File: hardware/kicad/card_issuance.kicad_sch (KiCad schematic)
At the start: 0 parts

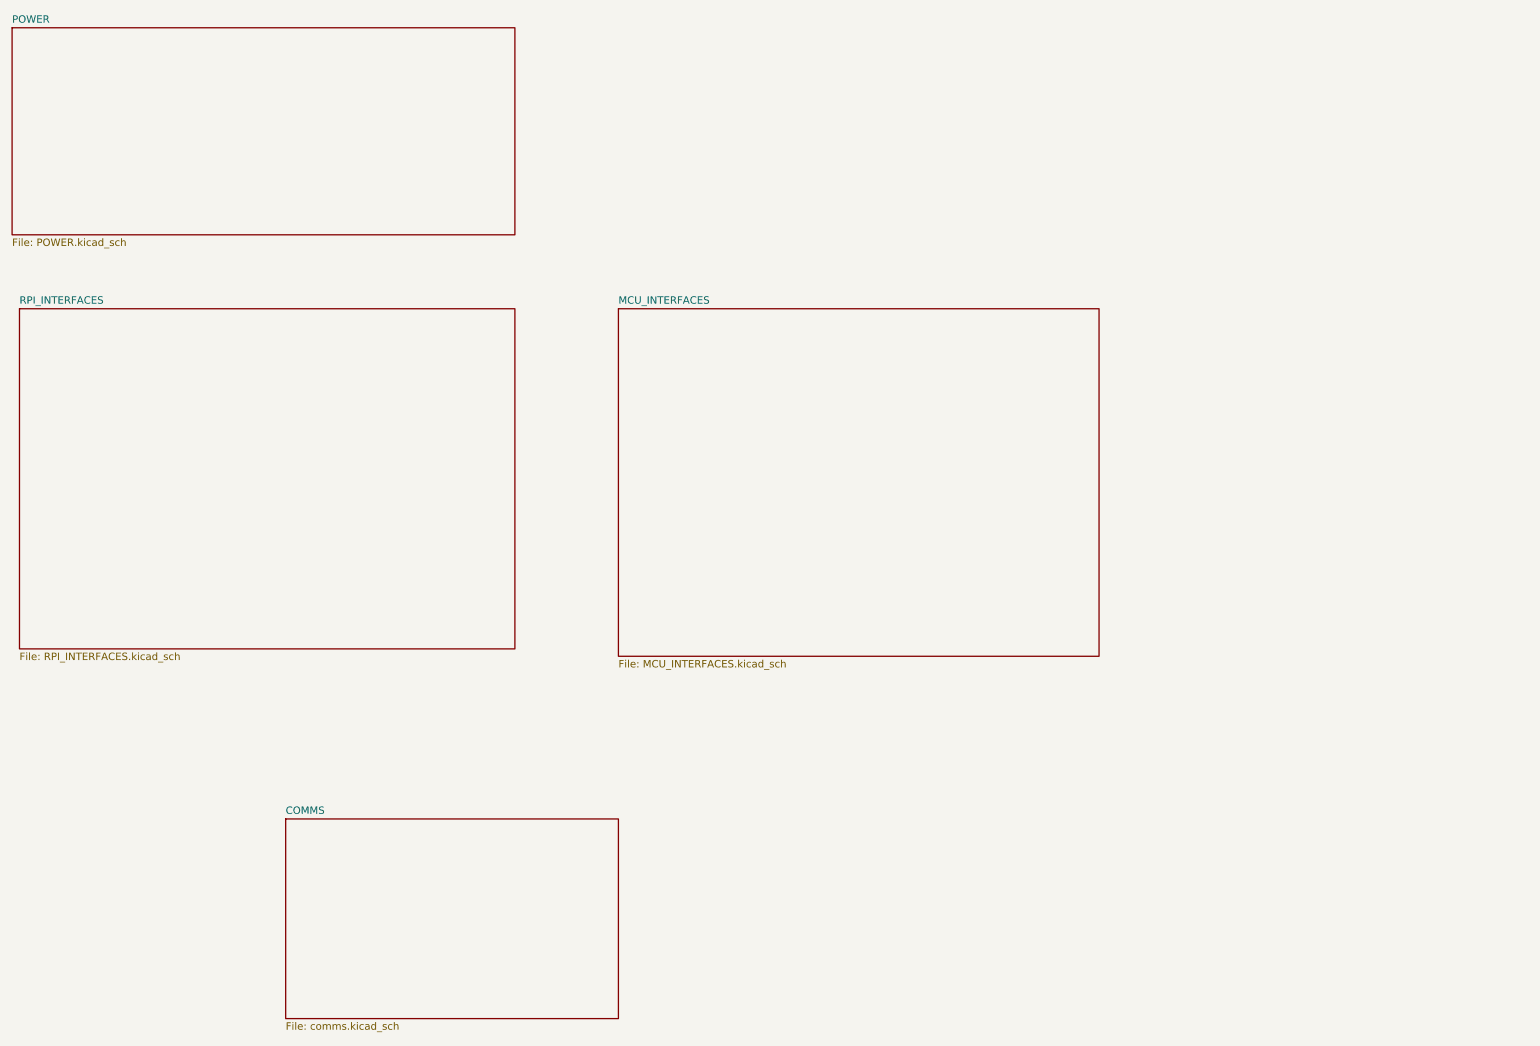
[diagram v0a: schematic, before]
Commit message: feat: mcu interfaces & motor connections
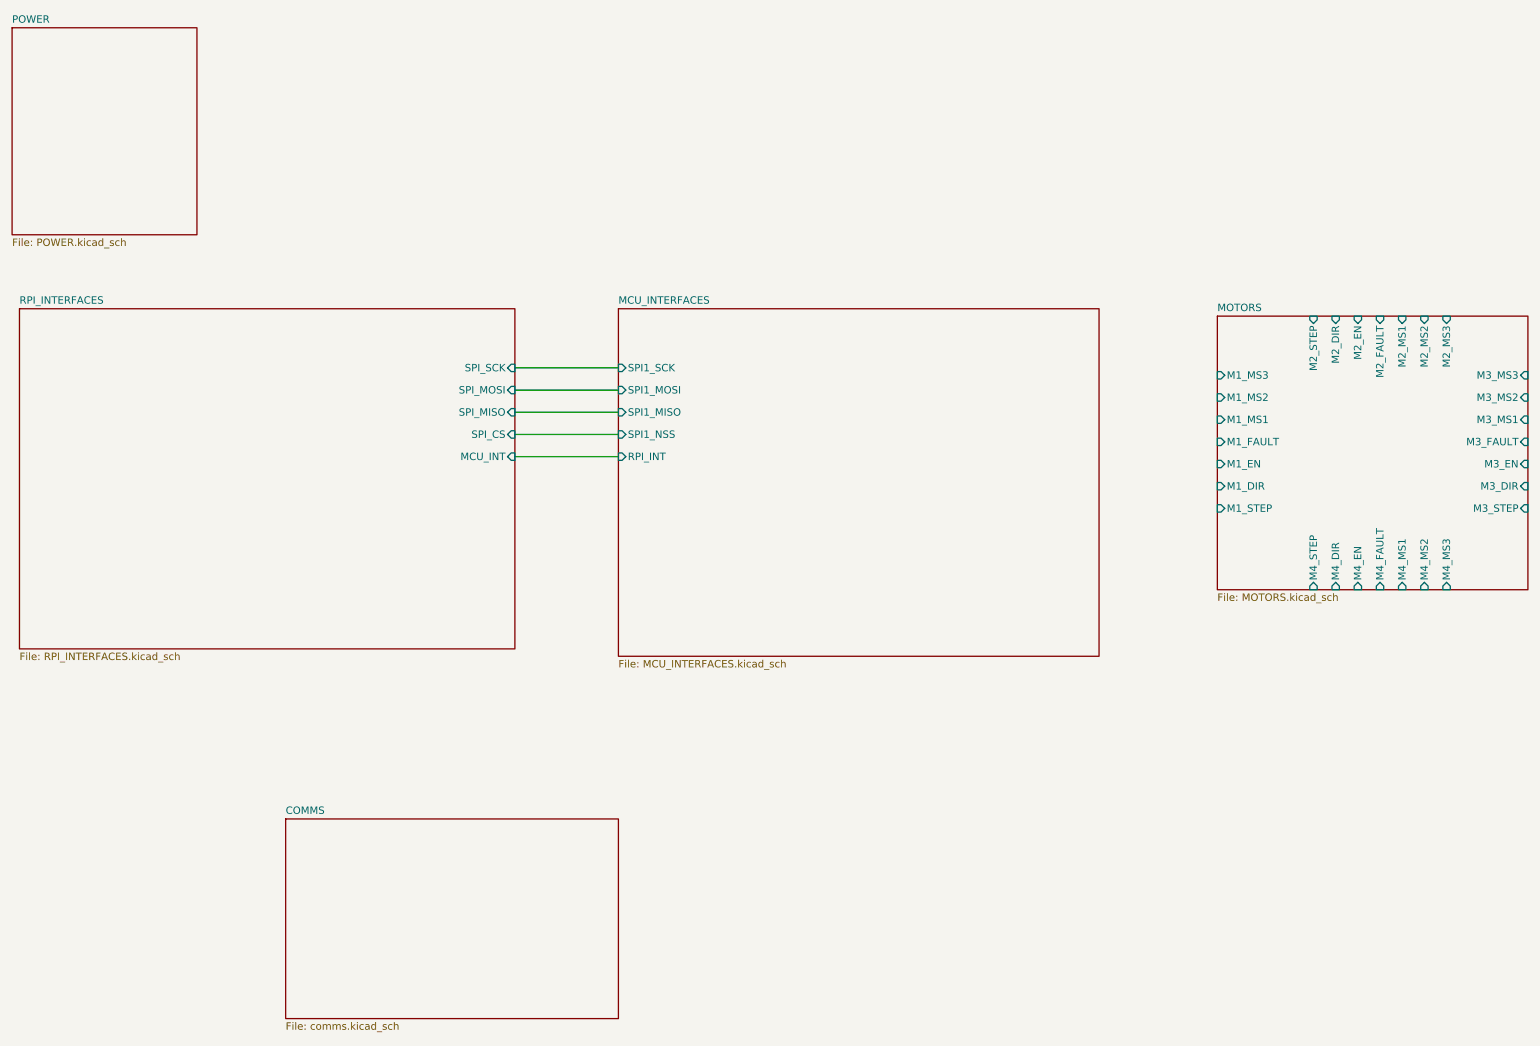
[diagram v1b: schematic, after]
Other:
- added sheet MOTORS (MOTORS.kicad_sch)
- sheet MCU_INTERFACES ports: added RPI_INT, SPI1_MISO, SPI1_MOSI, SPI1_NSS, SPI1_SCK; removed none
- sheet RPI_INTERFACES ports: added MCU_INT, SPI_CS, SPI_MISO, SPI_MOSI, SPI_SCK; removed none

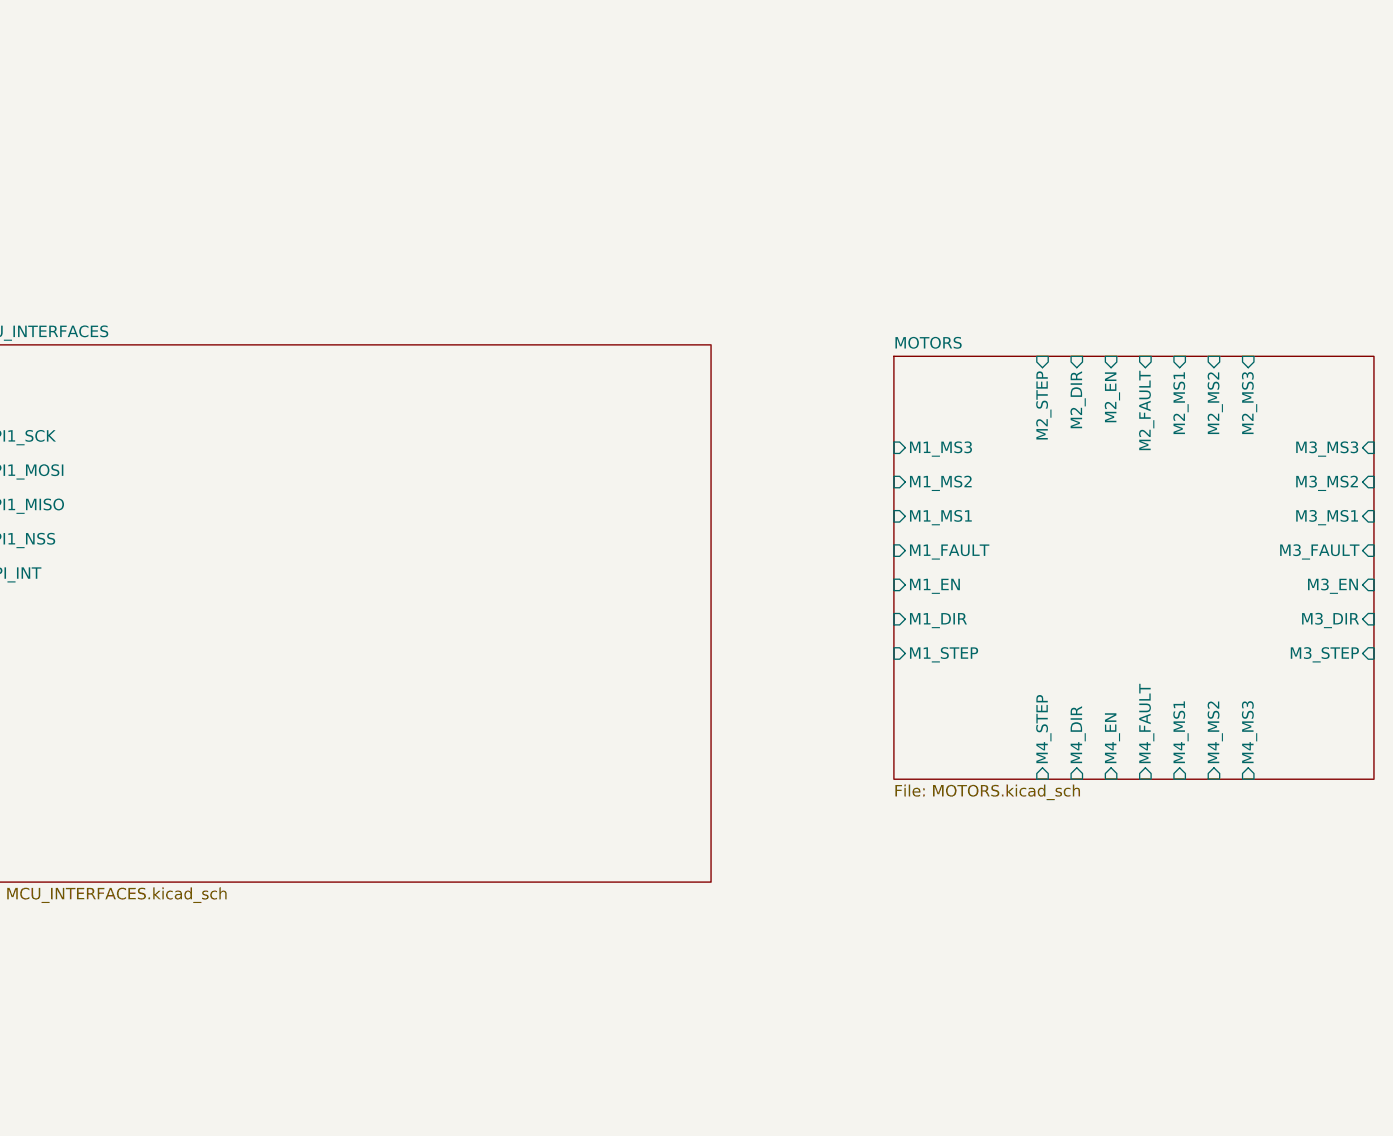
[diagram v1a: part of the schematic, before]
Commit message: feat: implemented keypad & reverse polarity protection
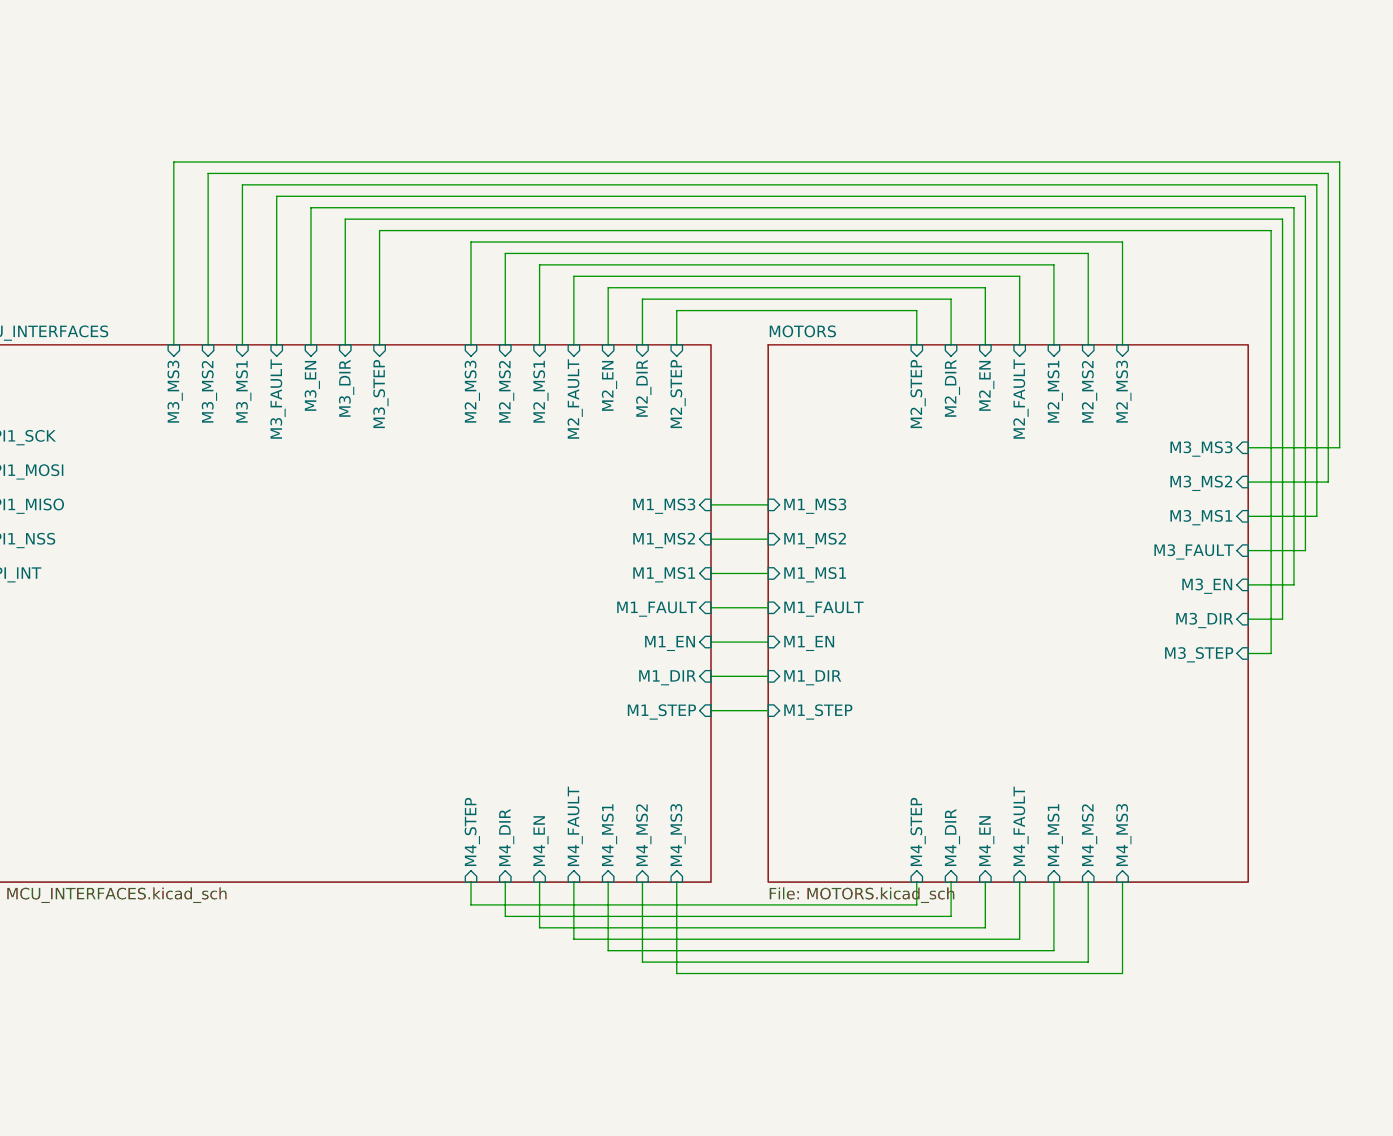
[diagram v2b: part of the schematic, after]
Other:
- sheet MCU_INTERFACES ports: added M1_DIR, M1_EN, M1_FAULT, M1_MS1, M1_MS2, M1_MS3, M1_STEP, M2_DIR, M2_EN, M2_FAULT, M2_MS1, M2_MS2, M2_MS3, M2_STEP, M3_DIR, M3_EN, M3_FAULT, M3_MS1, M3_MS2, M3_MS3, M3_STEP, M4_DIR, M4_EN, M4_FAULT, M4_MS1, M4_MS2, M4_MS3, M4_STEP; removed none
